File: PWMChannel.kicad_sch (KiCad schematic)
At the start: 6 parts, among them J501 WAGO-2065, J502 WAGO-2065, Q501 BSC010N04LS

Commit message: Update parts
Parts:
- C501: footprint Capacitor_SMD:C_0603_1608Metric -> V2_Capacitor_SMD:C_0603; symbol Device:C_Small -> V2_Device:C_0603_0u1; Manufacturer (none) -> TDK; Mouser (none) -> 810-CGA3E2X7R1H104MA; Product (none) -> CGA3E2X7R1H104M080AA
- D501: footprint Diode_SMD:D_SOD-123F -> V2_Diode_SMD:D_SOD-123F; Manufacturer (none) -> onsemi; Mouser (none) -> 512-S310FA; Product (none) -> S310FA
- D502: LCSC (none) -> C965555; Manufacturer (none) -> Worldsemi; Product (none) -> WS2812B-2020
- J501, J502: value WAGO-2065 -> WAGO 2065-100; Manufacturer (none) -> WAGO; Product (none) -> 2065-100/998-403
- Q501: Manufacturer (none) -> Infineon Technologies; Mouser (none) -> 726-BSC010N04LS; Product (none) -> BSC010N04LS
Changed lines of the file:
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@@
 			)
 		)
-		(property "Footprint" "Diode_SMD:D_SOD-123F"
+		(property "Footprint" "V2_Diode_SMD:D_SOD-123F"
 			(at 139.065 88.9 0)
 			(effects
@@
 		(property "Description" ""
 			(at 146.05 88.9 0)
+			(effects
+				(font
+					(size 1.27 1.27)
+				)
+				(hide yes)
+			)
+		)
+		(property "Mouser" "512-S310FA"
+			(at 135.89 88.9 0)
+			(effects
+				(font
+					(size 1.27 1.27)
+				)
+				(hide yes)
+			)
+		)
+		(property "Sim.Pin" ""
+			(at 146.05 88.9 90)
+			(effects
+				(font
+					(size 1.27 1.27)
+				)
+				(hide yes)
+			)
+		)
+		(property "Manufacturer" "onsemi"
+			(at 135.89 88.9 0)
+			(effects
+				(font
+					(size 1.27 1.27)
+				)
+				(hide yes)
+			)
+		)
+		(property "Product" "S310FA"
+			(at 133.35 88.9 0)
 			(effects
 				(font
@@
 	)
 	(symbol
-		(lib_id "Device:C_Small")
+		(lib_id "V2_Device:C_0603_0u1")
 		(at 133.35 88.9 0)
 		(unit 1)
@@
 			)
 		)
-		(property "Footprint" "Capacitor_SMD:C_0603_1608Metric"
+		(property "Footprint" "V2_Capacitor_SMD:C_0603"
+			(at 133.35 105.918 0)
+			(effects
+				(font
+					(size 1.27 1.27)
+				)
+				(hide yes)
+			)
+		)
+		(property "Datasheet" ""
 			(at 133.35 88.9 0)
 			(effects
@@
 			)
 		)
-		(property "Datasheet" "~"
+		(property "Description" "Unpolarized capacitor, small symbol"
+			(at 133.35 102.362 0)
+			(effects
+				(font
+					(size 1.27 1.27)
+				)
+				(hide yes)
+			)
+		)
+		(property "Mouser" "810-CGA3E2X7R1H104MA"
+			(at 133.35 106.172 0)
+			(effects
+				(font
+					(size 1.27 1.27)
+				)
+				(hide yes)
+			)
+		)
+		(property "Sim.Pin" ""
 			(at 133.35 88.9 0)
 			(effects
@@
 			)
 		)
-		(property "Description" "Unpolarized capacitor, small symbol"
-			(at 133.35 88.9 0)
+		(property "Manufacturer" "TDK"
+			(at 133.35 104.14 0)
+			(effects
+				(font
+					(size 1.27 1.27)
+				)
+				(hide yes)
+			)
+		)
+		(property "Product" "CGA3E2X7R1H104M080AA"
+			(at 133.35 106.68 0)
 			(effects
 				(font
@@
 			)
 		)
+		(property "Mouser" "726-BSC010N04LS"
+			(at 130.81 112.268 0)
+			(effects
+				(font
+					(size 1.27 1.27)
+				)
+				(hide yes)
+			)
+		)
+		(property "Sim.Pin" ""
+			(at 130.81 96.52 0)
+			(effects
+				(font
+					(size 1.27 1.27)
+				)
+				(hide yes)
+			)
+		)
+		(property "Product" "BSC010N04LS"
+			(at 130.81 116.84 0)
+			(effects
+				(font
+					(size 1.27 1.27)
+				)
+				(hide yes)
+			)
+		)
+		(property "Manufacturer" "Infineon Technologies"
+			(at 130.81 114.3 0)
+			(effects
+				(font
+					(size 1.27 1.27)
+				)
+				(hide yes)
+			)
+		)
 		(pin "1"
 		)
@@
 	)
 	(symbol
-		(lib_id "power:GND")
+		(lib_id "V2_power:GND")
 		(at 160.02 127 90)
 		(unit 1)
@@
 			)
 		)
+		(property "Manufacturer" "Worldsemi"
+			(at 152.4 141.224 0)
+			(effects
+				(font
+					(size 1.27 1.27)
+				)
+				(hide yes)
+			)
+		)
+		(property "Product" "WS2812B-2020"
+			(at 152.4 138.684 0)
+			(effects
+				(font
+					(size 1.27 1.27)
+				)
+				(hide yes)
+			)
+		)
+		(property "LCSC" "C965555"
+			(at 152.4 144.018 0)
+			(effects
+				(font
+					(size 1.27 1.27)
+				)
+				(hide yes)
+			)
+		)
+		(property "Sim.Pin" ""
+			(at 152.4 125.73 0)
+			(effects
+				(font
+					(size 1.27 1.27)
+				)
+				(hide yes)
+			)
+		)
 		(pin "1"
 		)
@@
 		(at 175.26 86.36 0)
 		(unit 1)
-		(exclude_from_sim yes)
+		(exclude_from_sim no)
 		(in_bom yes)
 		(on_board yes)
@@
 			)
 		)
-		(property "Value" "WAGO-2065"
+		(property "Value" "WAGO 2065-100"
 			(at 175.26 92.71 0)
 			(effects
@@
 					(size 1.27 1.27)
 				)
-				(hide yes)
 			)
 		)
@@
 			)
 		)
-		(property "Datasheet" "~"
+		(property "Datasheet" ""
 			(at 175.26 90.17 0)
 			(effects
@@
 		)
 		(property "Description" ""
+			(at 175.26 86.36 0)
+			(effects
+				(font
+					(size 1.27 1.27)
+				)
+				(hide yes)
+			)
+		)
+		(property "Manufacturer" "WAGO"
+			(at 175.26 99.568 0)
+			(effects
+				(font
+					(size 1.27 1.27)
+				)
+				(hide yes)
+			)
+		)
+		(property "Product" "2065-100/998-403"
+			(at 175.26 102.87 0)
+			(effects
+				(font
+					(size 1.27 1.27)
+				)
+				(hide yes)
+			)
+		)
+		(property "Sim.Pin" ""
 			(at 175.26 86.36 0)
 			(effects
@@
 	)
 	(symbol
-		(lib_id "power:GND")
+		(lib_id "V2_power:GND")
 		(at 133.35 101.6 0)
 		(unit 1)
@@
 		(at 175.26 91.44 0)
 		(unit 1)
-		(exclude_from_sim yes)
+		(exclude_from_sim no)
 		(in_bom yes)
 		(on_board yes)
@@
 			)
 		)
-		(property "Value" "WAGO-2065"
+		(property "Value" "WAGO 2065-100"
 			(at 175.26 97.79 0)
 			(effects
@@
 					(size 1.27 1.27)
 				)
-				(hide yes)
 			)
 		)
@@
 			)
 		)
-		(property "Datasheet" "~"
+		(property "Datasheet" ""
 			(at 175.26 95.25 0)
 			(effects
@@
 		)
 		(property "Description" ""
+			(at 175.26 91.44 0)
+			(effects
+				(font
+					(size 1.27 1.27)
+				)
+				(hide yes)
+			)
+		)
+		(property "Manufacturer" "WAGO"
+			(at 175.26 104.648 0)
+			(effects
+				(font
+					(size 1.27 1.27)
+				)
+				(hide yes)
+			)
+		)
+		(property "Product" "2065-100/998-403"
+			(at 175.26 107.95 0)
+			(effects
+				(font
+					(size 1.27 1.27)
+				)
+				(hide yes)
+			)
+		)
+		(property "Sim.Pin" ""
 			(at 175.26 91.44 0)
 			(effects
@@
 	)
 	(symbol
-		(lib_id "power:+5V")
+		(lib_id "V2_power:+5V")
 		(at 160.02 121.92 270)
 		(unit 1)

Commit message: Update library
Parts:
- C501: Rating (none) -> 50V
- Q501: Polarity (none) -> N; Rating (none) -> 40V
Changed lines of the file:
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@@
-			)
-		)
-		(property "Sim.Pin" ""
-			(at 146.05 88.9 90)
-			(effects
-				(font
-					(size 1.27 1.27)
-				)
-				(hide yes)
 			)
 		)
@@
 			)
 		)
-		(property "Sim.Pin" ""
-			(at 133.35 88.9 0)
-			(effects
-				(font
-					(size 1.27 1.27)
-				)
-				(hide yes)
-			)
-		)
 		(property "Manufacturer" "TDK"
 			(at 133.35 104.14 0)
@@
 		(property "Product" "CGA3E2X7R1H104M080AA"
 			(at 133.35 106.68 0)
+			(effects
+				(font
+					(size 1.27 1.27)
+				)
+				(hide yes)
+			)
+		)
+		(property "Rating" "50V"
+			(at 133.35 111.76 0)
 			(effects
 				(font
@@
 			)
 		)
-		(property "Sim.Pin" ""
-			(at 130.81 96.52 0)
-			(effects
-				(font
-					(size 1.27 1.27)
-				)
-				(hide yes)
-			)
-		)
 		(property "Product" "BSC010N04LS"
 			(at 130.81 116.84 0)
@@
 		)
 		(property "Manufacturer" "Infineon Technologies"
+			(at 130.81 114.3 0)
+			(effects
+				(font
+					(size 1.27 1.27)
+				)
+				(hide yes)
+			)
+		)
+		(property "Rating" "40V"
+			(at 130.81 116.84 0)
+			(effects
+				(font
+					(size 1.27 1.27)
+				)
+				(hide yes)
+			)
+		)
+		(property "Polarity" "N"
 			(at 130.81 114.3 0)
 			(effects
@@
 			)
 		)
-		(property "Description" "Power symbol creates a global label with name \"GND\" , ground"
+		(property "Description" ""
 			(at 160.02 127 0)
 			(effects
@@
 			)
 		)
-		(property "Sim.Pin" ""
-			(at 152.4 125.73 0)
-			(effects
-				(font
-					(size 1.27 1.27)
-				)
-				(hide yes)
-			)
-		)
 		(pin "1"
 		)
@@
 			)
 		)
-		(property "Sim.Pin" ""
-			(at 175.26 86.36 0)
-			(effects
-				(font
-					(size 1.27 1.27)
-				)
-				(hide yes)
-			)
-		)
 		(pin "1"
 		)
@@
 			)
 		)
-		(property "Description" "Power symbol creates a global label with name \"GND\" , ground"
+		(property "Description" ""
 			(at 133.35 101.6 0)
 			(effects
@@
 			)
 		)
-		(property "Sim.Pin" ""
-			(at 175.26 91.44 0)
-			(effects
-				(font
-					(size 1.27 1.27)
-				)
-				(hide yes)
-			)
-		)
 		(pin "1"
 		)
@@
 			)
 		)
-		(property "Description" "Power symbol creates a global label with name \"+5V\""
+		(property "Description" ""
 			(at 160.02 121.92 0)
 			(effects

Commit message: Update Library
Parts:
- C501: symbol V2_Device:C_0603_0u1 -> V2_Capacitor:0603_0u1
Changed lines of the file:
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@@
 	)
 	(symbol
-		(lib_id "V2_Device:C_0603_0u1")
+		(lib_id "V2_Capacitor:0603_0u1")
 		(at 133.35 88.9 0)
 		(unit 1)

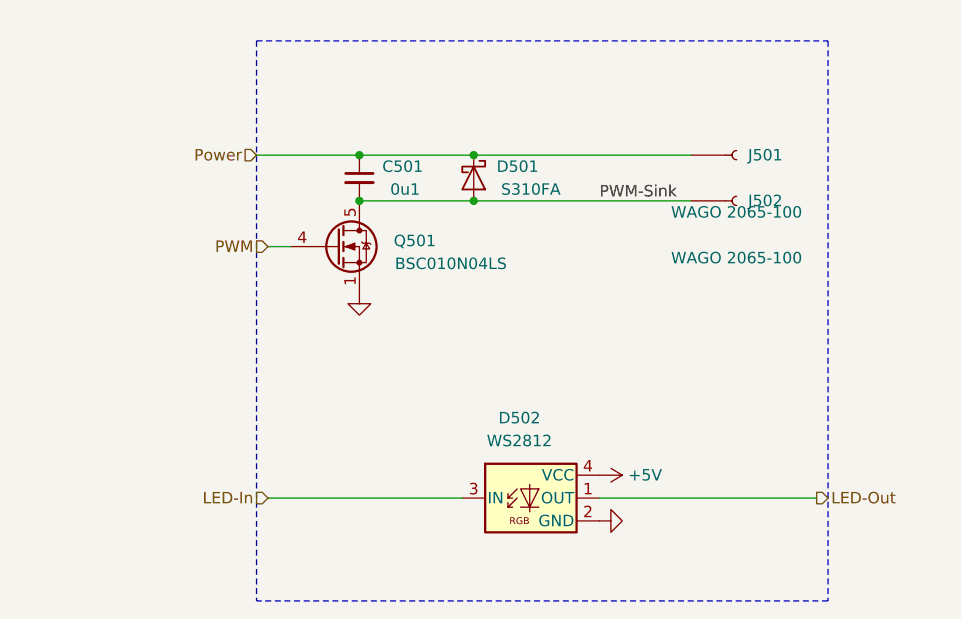
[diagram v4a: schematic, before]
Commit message: Replace diode
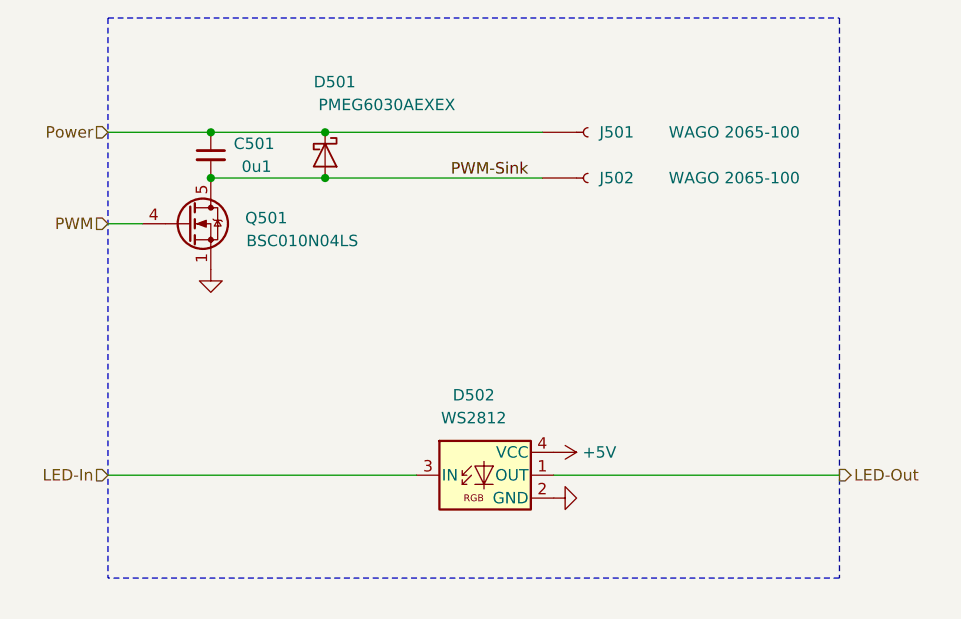
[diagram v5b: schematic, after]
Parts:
- D501: value S310FA -> PMEG6030AEXEX; footprint V2_Diode_SMD:D_SOD-123F -> V2_Diode_SMD:D_SOD-123HP; symbol V2_Diode:S310FA -> V2_Diode:PMEG6030AEXEX; Manufacturer onsemi -> Nexperia; Mouser 512-S310FA -> 771-PMEG6030AEXEX; Product S310FA -> PMEG6030AEXEX
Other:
- moved on the sheet: C501, D501, D502, J501, J502, Q501

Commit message: Update ESD suppressor
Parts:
- D501: Rating (none) -> 60V
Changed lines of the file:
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@@
+			)
+		)
+		(property "Rating" "60V"
+			(at 111.76 86.36 0)
+			(effects
+				(font
+					(size 1.27 1.27)
+				)
+				(hide yes)
 			)
 		)

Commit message: Replace diode
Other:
- title: Solenoid Channel -> V2 drum

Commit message: Update
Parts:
- C501: Id (none) -> Capacitor:${SYMBOL_NAME}
- D501: Id (none) -> Diode:${SYMBOL_NAME}
- D502: Id (none) -> LED:${SYMBOL_NAME}; Rating (none) -> 15mA
- J501, J502: Id (none) -> WAGO:${SYMBOL_NAME}; Rating (none) -> 9A
- Q501: Id (none) -> MOSFET:${SYMBOL_NAME}; Polarity N -> (none)
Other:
- company: Power MOSFET + RGB LED -> Versio Duo
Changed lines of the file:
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@@
 	(title_block
 		(title "V2 drum")
-		(date "2026-03-30")
+		(date "2026-04-14")
 		(rev "2026-03-30")
-		(company "Power MOSFET + RGB LED")
+		(company "Versio Duo")
+		(comment 1 "Percussion Controller")
 	)
 	(junction
@@
 			)
 		)
+		(property "Id" "Diode:${SYMBOL_NAME}"
+			(at 118.11 86.36 0)
+			(hide yes)
+			(show_name no)
+			(do_not_autoplace no)
+			(effects
+				(font
+					(size 1.27 1.27)
+				)
+			)
+		)
 		(pin "1"
 		)
@@
 			)
 		)
+		(property "Id" "Capacitor:${SYMBOL_NAME}"
+			(at 116.84 101.6 0)
+			(hide yes)
+			(show_name no)
+			(do_not_autoplace no)
+			(effects
+				(font
+					(size 1.27 1.27)
+				)
+			)
+		)
 		(pin "1"
 		)
@@
 			)
 		)
-		(property "Polarity" "N"
-			(at 114.3 111.76 0)
+		(property "Id" "MOSFET:${SYMBOL_NAME}"
+			(at 114.3 109.22 0)
 			(hide yes)
 			(show_name no)
@@
 		(in_pos_files yes)
 		(dnp no)
-		(property "Reference" "#PWR503"
+		(property "Reference" "#PWR0503"
 			(at 161.29 124.46 0)
 			(hide yes)
@@
 			(project "drum"
 				(path "/6c8448b4-b04d-47e1-934e-e40cbe27a7be/c0032080-b223-4ef5-af6e-f10445519ca7"
-					(reference "#PWR603")
+					(reference "#PWR0603")
 					(unit 1)
 				)
 				(path "/6c8448b4-b04d-47e1-934e-e40cbe27a7be/ecb8eef8-bb26-4217-a3d3-147bd9b06112"
-					(reference "#PWR503")
+					(reference "#PWR0503")
 					(unit 1)
 				)
@@
 			)
 		)
+		(property "Id" "LED:${SYMBOL_NAME}"
+			(at 147.32 132.08 0)
+			(hide yes)
+			(show_name no)
+			(do_not_autoplace no)
+			(effects
+				(font
+					(size 1.27 1.27)
+				)
+			)
+		)
+		(property "Rating" "15mA"
+			(at 147.32 147.32 0)
+			(hide yes)
+			(show_name no)
+			(do_not_autoplace no)
+			(effects
+				(font
+					(size 1.27 1.27)
+				)
+			)
+		)
 		(pin "1"
 		)
@@
 			)
 		)
+		(property "Id" "WAGO:${SYMBOL_NAME}"
+			(at 158.75 91.44 0)
+			(hide yes)
+			(show_name no)
+			(do_not_autoplace no)
+			(effects
+				(font
+					(size 1.27 1.27)
+				)
+			)
+		)
+		(property "Rating" "9A"
+			(at 158.75 101.6 0)
+			(hide yes)
+			(show_name no)
+			(do_not_autoplace no)
+			(effects
+				(font
+					(size 1.27 1.27)
+				)
+			)
+		)
 		(pin "1"
 		)
@@
 		(in_pos_files yes)
 		(dnp no)
-		(property "Reference" "#PWR501"
+		(property "Reference" "#PWR0501"
 			(at 116.84 105.41 0)
 			(hide yes)
@@
 			(project "drum"
 				(path "/6c8448b4-b04d-47e1-934e-e40cbe27a7be/c0032080-b223-4ef5-af6e-f10445519ca7"
-					(reference "#PWR601")
+					(reference "#PWR0601")
 					(unit 1)
 				)
 				(path "/6c8448b4-b04d-47e1-934e-e40cbe27a7be/ecb8eef8-bb26-4217-a3d3-147bd9b06112"
-					(reference "#PWR501")
+					(reference "#PWR0501")
 					(unit 1)
 				)
@@
 			)
 		)
+		(property "Id" "WAGO:${SYMBOL_NAME}"
+			(at 158.75 96.52 0)
+			(hide yes)
+			(show_name no)
+			(do_not_autoplace no)
+			(effects
+				(font
+					(size 1.27 1.27)
+				)
+			)
+		)
+		(property "Rating" "9A"
+			(at 158.75 106.68 0)
+			(hide yes)
+			(show_name no)
+			(do_not_autoplace no)
+			(effects
+				(font
+					(size 1.27 1.27)
+				)
+			)
+		)
 		(pin "1"
 		)
@@
 		(in_pos_files yes)
 		(dnp no)
-		(property "Reference" "#PWR502"
+		(property "Reference" "#PWR0502"
 			(at 151.13 119.38 0)
 			(hide yes)
@@
 			(project "drum"
 				(path "/6c8448b4-b04d-47e1-934e-e40cbe27a7be/c0032080-b223-4ef5-af6e-f10445519ca7"
-					(reference "#PWR602")
+					(reference "#PWR0602")
 					(unit 1)
 				)
 				(path "/6c8448b4-b04d-47e1-934e-e40cbe27a7be/ecb8eef8-bb26-4217-a3d3-147bd9b06112"
-					(reference "#PWR502")
-					(unit 1)
-				)
+					(reference "#PWR0502")
+					(unit 1)
+				)
